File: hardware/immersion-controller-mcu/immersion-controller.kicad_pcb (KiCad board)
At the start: 2 copper layers, 144.8 x 45.7 mm, 14 parts, among them J1 TANK-TOP, J2 TANK-BOTTOM, J3 COLD, J4 DISPLAY, J5 RTC, J7 MCU, SW2 RotaryEncoder_Switch, U1 ESP32-S3-DevKitC, U12 DHT11

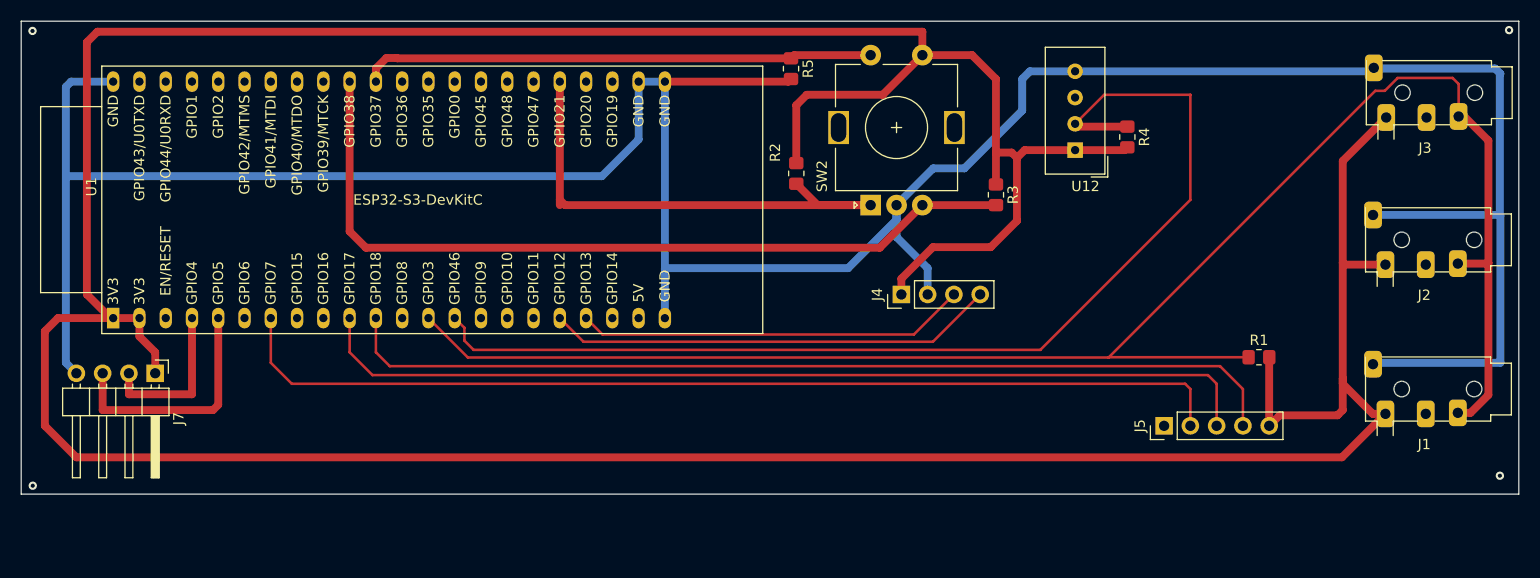
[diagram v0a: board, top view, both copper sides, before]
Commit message: Added missing pullup resistor and reset pin
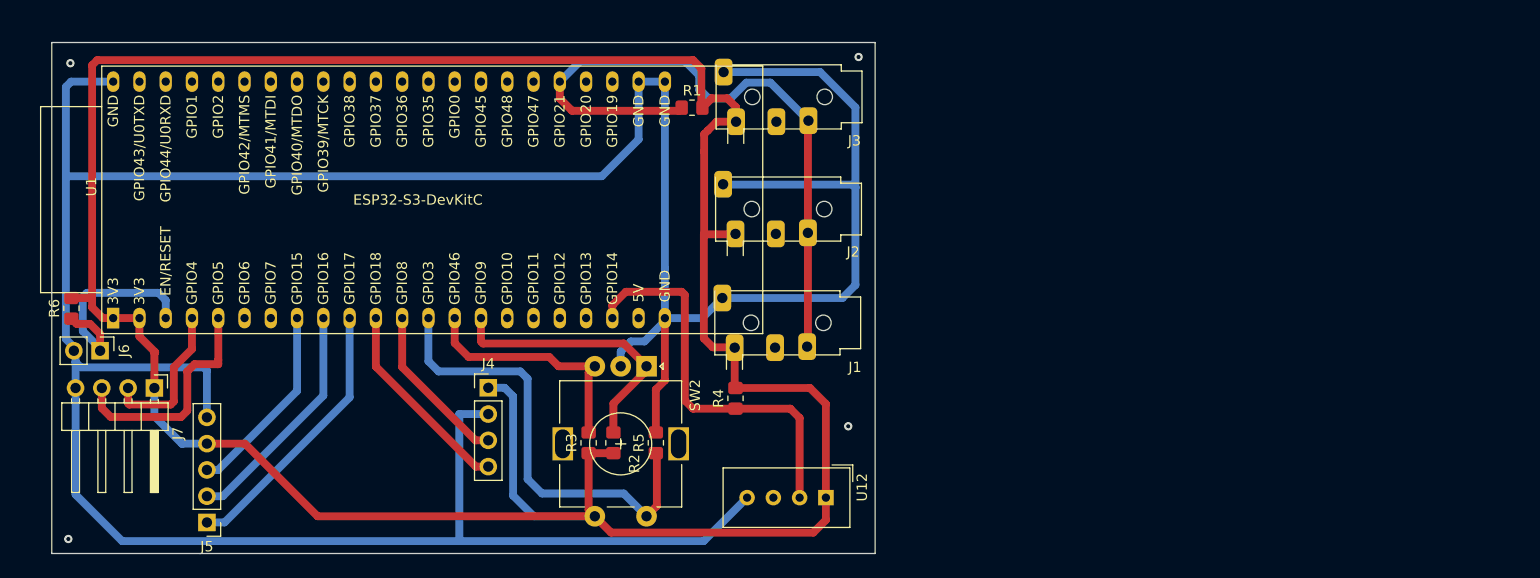
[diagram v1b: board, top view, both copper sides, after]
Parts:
- added J6: RESET, Connector_PinHeader_2.54mm:PinHeader_1x02_P2.54mm_Vertical, F.Cu at (20.1, 110.6)
- added R6: 4k7, Resistor_SMD:R_0805_2012Metric_Pad1.20x1.40mm_HandSolder, F.Cu at (17.3, 106.5)
- moved J5 93.0 mm to (30.4, 127.2), turned to 180 degrees
- moved J1 63.2 mm to (85.2, 107.9)
- moved J2 62.9 mm to (85.3, 96.9)
- moved J3 62.9 mm to (85.4, 86.1)
- moved R1 59.9 mm to (77.3, 87.1)
- moved R3 46.1 mm to (67.3, 119.5), turned to 90 degrees
- moved R4 45.5 mm to (81.5, 115.2), turned to 90 degrees
- moved U12 41.3 mm to (90.2, 124.8), turned to -90 degrees
- moved J4 40.9 mm to (57.6, 114.2), turned to 0 degrees
- moved R5 38.5 mm to (73.8, 119.5), turned to 90 degrees
- moved R2 31.5 mm to (69.7, 119.5), turned to 90 degrees
- moved SW2 26.7 mm to (72.9, 112.1), turned to -90 degrees
- moved J7 1.43 mm to (25.3, 114.2)
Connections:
- J5 pad 1: unconnected-(J5-Pin_1-Pad1) -> RTC_DS
- J5 pad 2: RTC_SQW -> RTC_SCK
- J5 pad 3: RTC_SCK -> RTC_SDA
- J5 pad 4: RTC_SDA -> +3.3V
- J5 pad 5: +3.3V -> GND
- U1 pad 10: RTC_SCK -> RTC_DS
- U1 pad 11: RTC_SDA -> DISPLAY_SDA
- U1 pad 12: unconnected-(U1-GPIO8/ADC1_CH7-Pad12) -> DISPLAY_SCL
- U1 pad 13: WATERTEMP_DATA -> ROT_SW
- U1 pad 14: DHT_DATA -> ROT_DT
- U1 pad 15: unconnected-(U1-GPIO9/ADC1_CH8-Pad15) -> ROT_CLK
- U1 pad 18: DISPLAY_SDA -> unconnected-(U1-GPIO12/ADC2_CH1-Pad18)
- U1 pad 19: DISPLAY_SCL -> unconnected-(U1-GPIO13/ADC2_CH2-Pad19)
- U1 pad 20: unconnected-(U1-GPIO14/ADC2_CH3-Pad20) -> DHT_DATA
- U1 pad 27: ROT_CLK -> WATERTEMP_DATA
- U1 pad 3: unconnected-(U1-CHIP_PU-Pad3) -> RST
- U1 pad 34: ROT_SW -> unconnected-(U1-GPIO37-Pad34)
- U1 pad 35: ROT_DT -> unconnected-(U1-GPIO38-Pad35)
- U1 pad 7: RTC_SQW -> unconnected-(U1-GPIO7/ADC1_CH6-Pad7)
- U1 pad 8: unconnected-(U1-GPIO15/ADC2_CH4/32K_P-Pad8) -> RTC_SDA
- U1 pad 9: unconnected-(U1-GPIO16/ADC2_CH5/32K_N-Pad9) -> RTC_SCK
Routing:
- net +3.3V: track 395.5 -> 263.7 mm
- net WATERTEMP_DATA: track 164.4 -> 65.3 mm
- net RTC_SQW: track 97.8 -> 0.00 mm
- net RTC_SDA: track 92.2 -> 18.9 mm
- net RTC_SCK: track 92.4 -> 22.8 mm
- net DHT_DATA: track 106.8 -> 38.6 mm
- net ROT_DT: track 79.3 -> 23.5 mm
- net GND: track 287.2 -> 316.2 mm
- net RTC_DS: track 0.00 -> 26.5 mm
- net DISPLAY_SDA: track 43.5 -> 19.6 mm
- net ROT_CLK: track 50.2 -> 27.0 mm
- net DISPLAY_SCL: track 37.8 -> 16.0 mm
- net RST: track 0.00 -> 21.1 mm
- net ROT_SW: track 49.7 -> 43.7 mm
- net RELAY_BOTTOM: track 23.3 -> 22.4 mm
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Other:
- board size 144.8 x 45.7 mm -> 79.6 x 49.4 mm
